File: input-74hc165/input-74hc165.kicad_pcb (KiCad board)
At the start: 2 copper layers, 32.1 x 21.5 mm, 6 parts, among them J1 Conn_01x10_Male

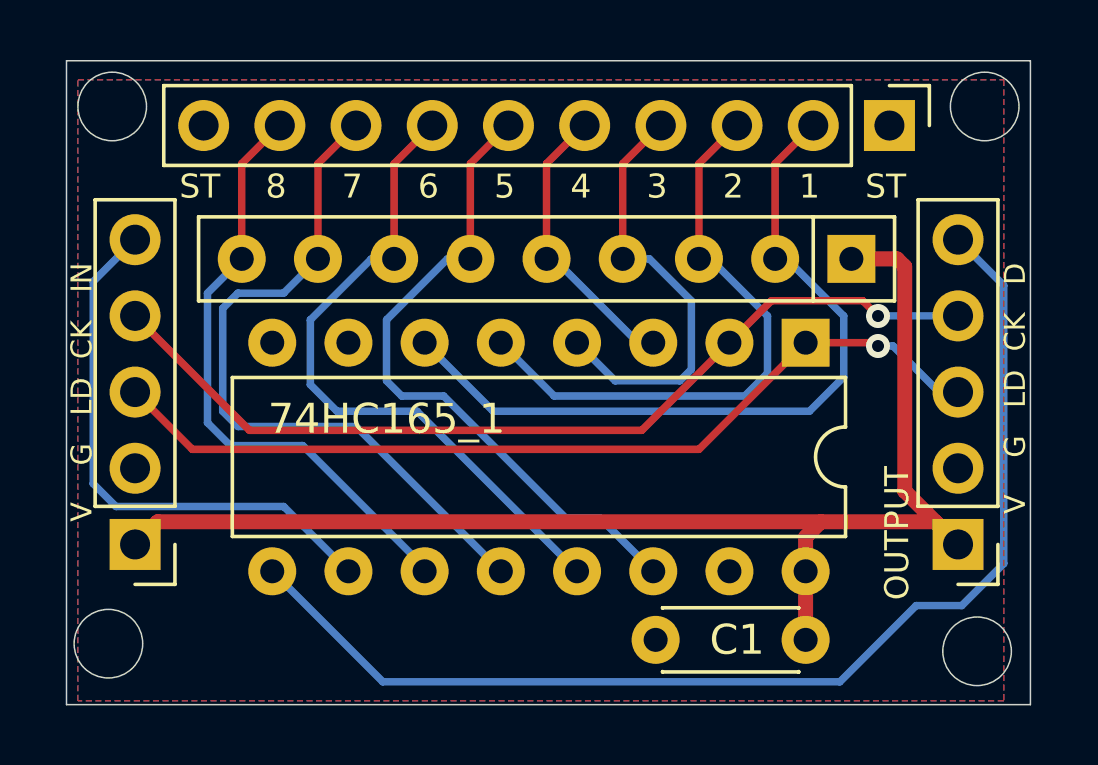
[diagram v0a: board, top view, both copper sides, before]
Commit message: 74hc165 보드 레이아웃 변경
Signed-off-by: Ju, Gyeong-min <jcmh74@gmail.com>
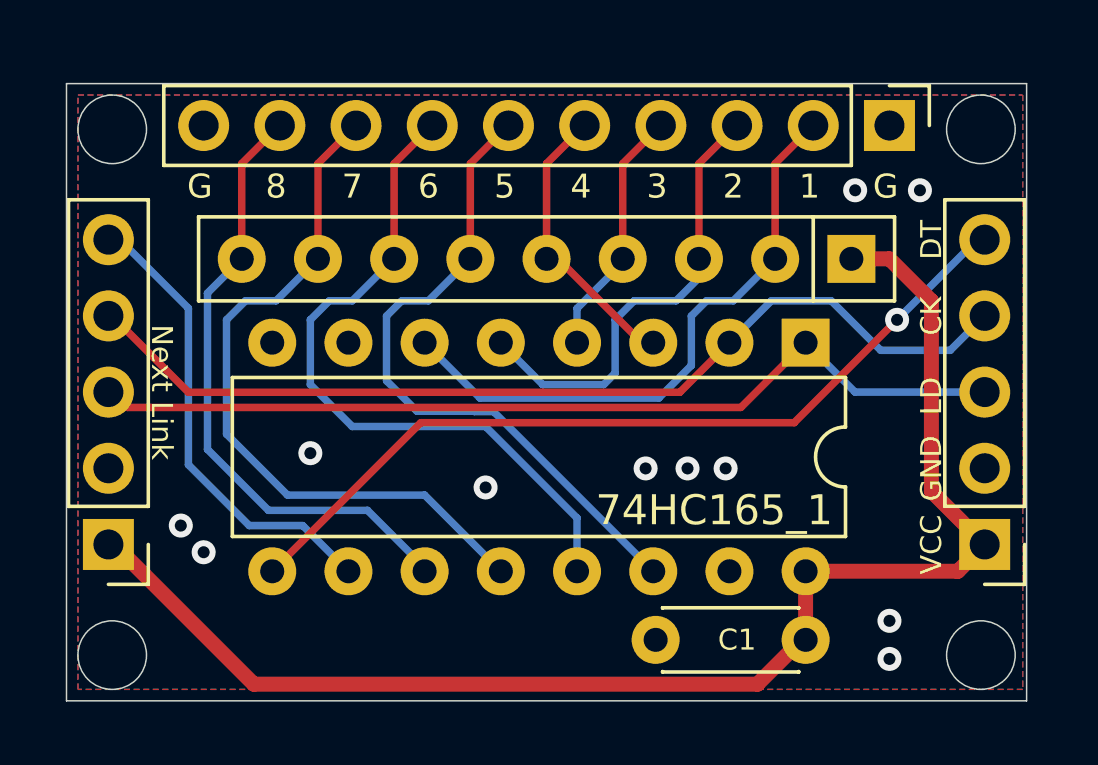
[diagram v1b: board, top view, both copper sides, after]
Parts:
- moved IN1 0.89 mm to (150.0, 100.3)
- moved OUT1 0.89 mm to (179.2, 100.3)
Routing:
- net /D_OUT: track 39.0 -> 28.3 mm, vias 0 -> 1
- net /C_3: track 14.6 -> 8.40 mm
- net /C_1: track 25.5 -> 20.3 mm
- net /C_2: track 19.9 -> 15.3 mm
- net /D_IN: track 18.4 -> 15.6 mm
- net VCC: track 44.1 -> 46.5 mm
- net /CLK: track 31.0 -> 32.7 mm, vias 1 -> 0
- net /C_6: track 22.2 -> 23.3 mm
- net /LOAD: track 30.4 -> 31.0 mm, vias 1 -> 0
- net /C_8: track 20.3 -> 20.8 mm
- net GND: vias 0 -> 11
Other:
- board size 32.1 x 21.5 mm -> 32 x 20.6 mm
- board text added: "CK"
- board text added: "DT"
- board text added: "G"
- board text added: "GND"
- board text added: "LD"
- board text added: "Next Link"
- board text added: "Rev.1"
- board text added: "VCC"
- board text removed: "OUTPUT"
- board text removed: "Rev.2"
- board text removed: "ST"
- board text removed: "V G LD CK D"
- board text removed: "V G LD CK IN"
